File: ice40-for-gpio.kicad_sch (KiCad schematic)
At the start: 25 parts, among them U10 W25Q128JVS, U6 LP5907MFX-1.2, U9 ICE40UP5K-SG48ITR

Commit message: Update the schematic
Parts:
- added D6, D7: RED, LED_SMD:LED_0603_1608Metric, symbol Device:LED_Small
- added R34, R35: 1.2K, Resistor_SMD:R_0402_1005Metric, symbol Device:R_Small
- renumbered C32 to C20, C42 to C21, C33 to C22, C43 to C23, C35 to C24, C36 to C25, C34 to C26, C37 to C27, C19 to C28, C38 to C29, C39 to C30, C40 to C31, C20 to C32, C41 to C33, D9 to D5, R36 to R32, R45 to R33, R37 to R36, R38 to R37, R39 to R38, R40 to R39, U9 to U6, U10 to U7, U6 to U8
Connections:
- net GND: now also D6.1 (K), D7.1 (K)
- net ICE_LED1: now also R34.1
- net ICE_LED2: now also R35.1
- new net: D6.2 (A), R34.2
- new net: D7.2 (A), R35.2

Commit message: Update the source code
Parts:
- renumbered C20 to C18, C21 to C19, C22 to C20, C23 to C21, C24 to C22, C25 to C23, C26 to C24, C27 to C25, C28 to C26, C29 to C27, C30 to C28, C31 to C29, C32 to C30, C33 to C31, R32 to R38, R33 to R39, R34 to R40, R35 to R41, R36 to R42, R37 to R43, R38 to R44, R39 to R45, U6 to U5, U7 to U6, U8 to U7

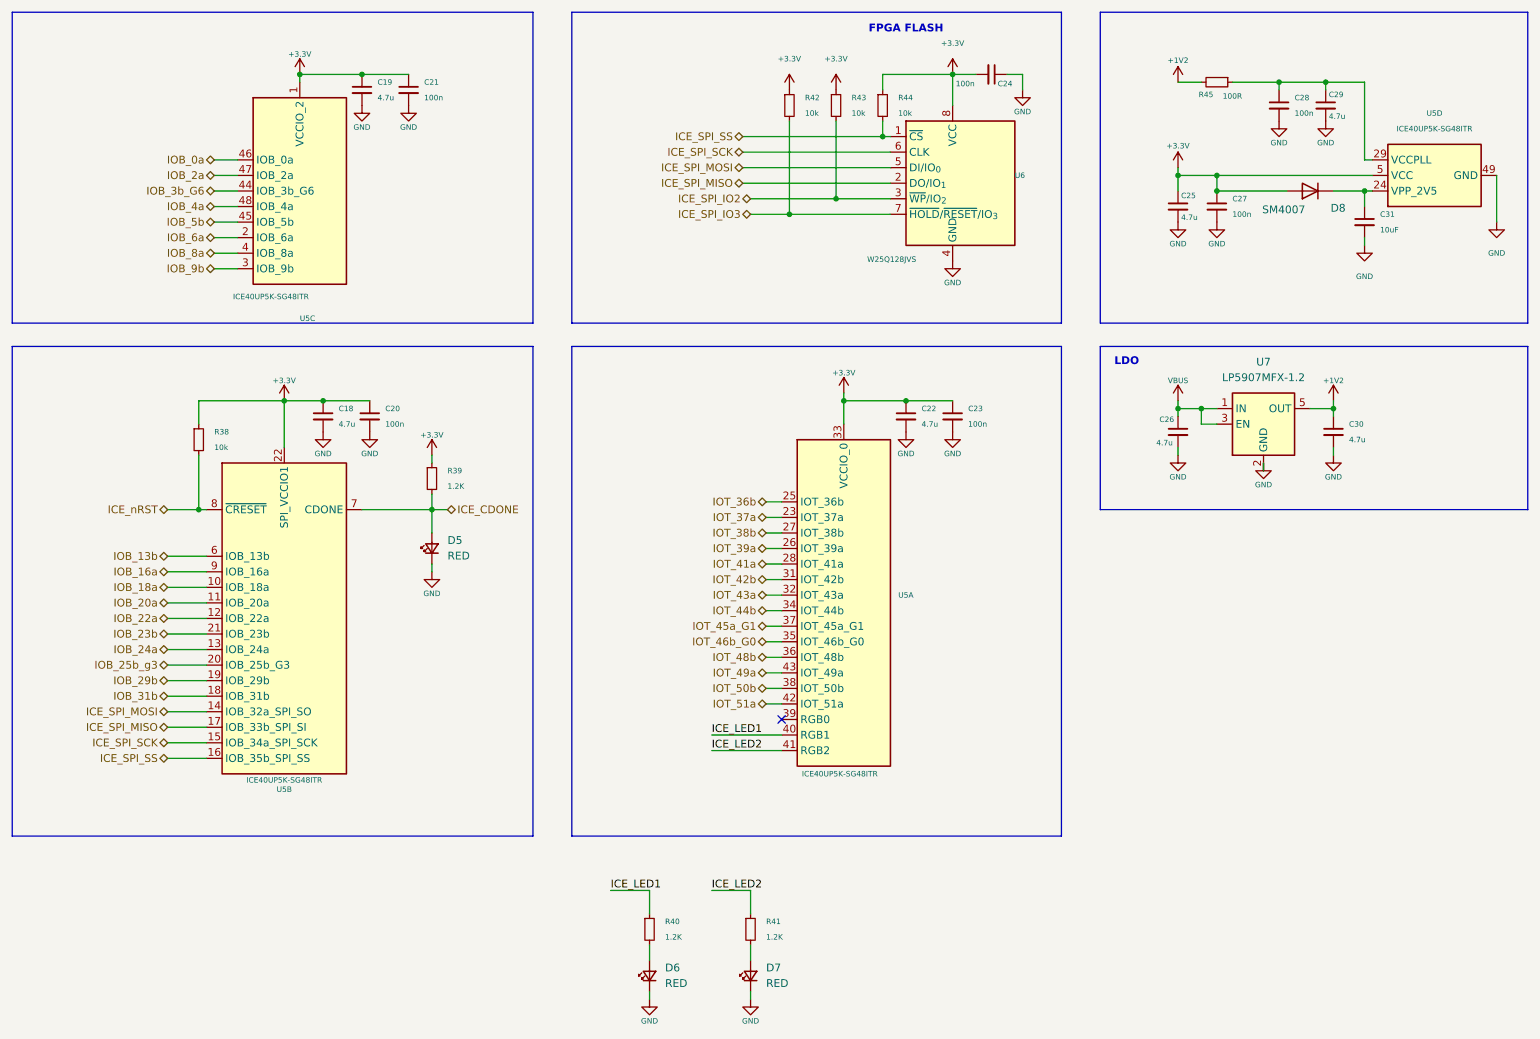
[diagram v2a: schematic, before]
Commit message: Update the footprints
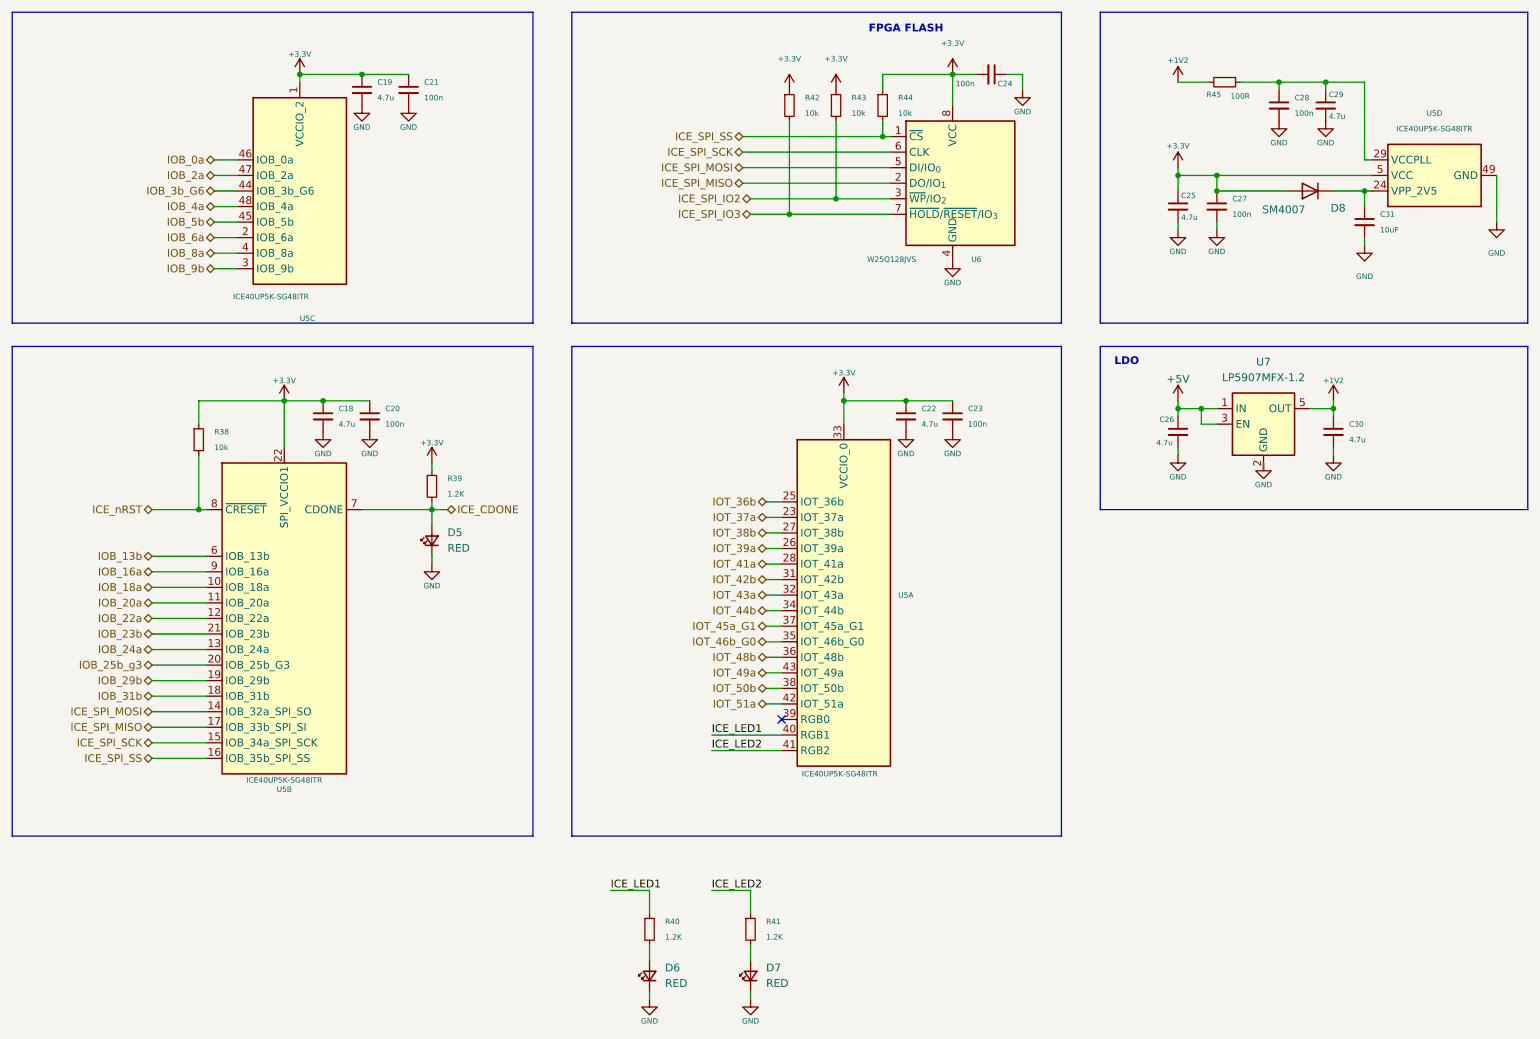
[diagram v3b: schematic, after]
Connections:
- net VBUS renamed +5V
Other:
- moved on the sheet: D5, R39, R45

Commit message: Update the BOM and the routing
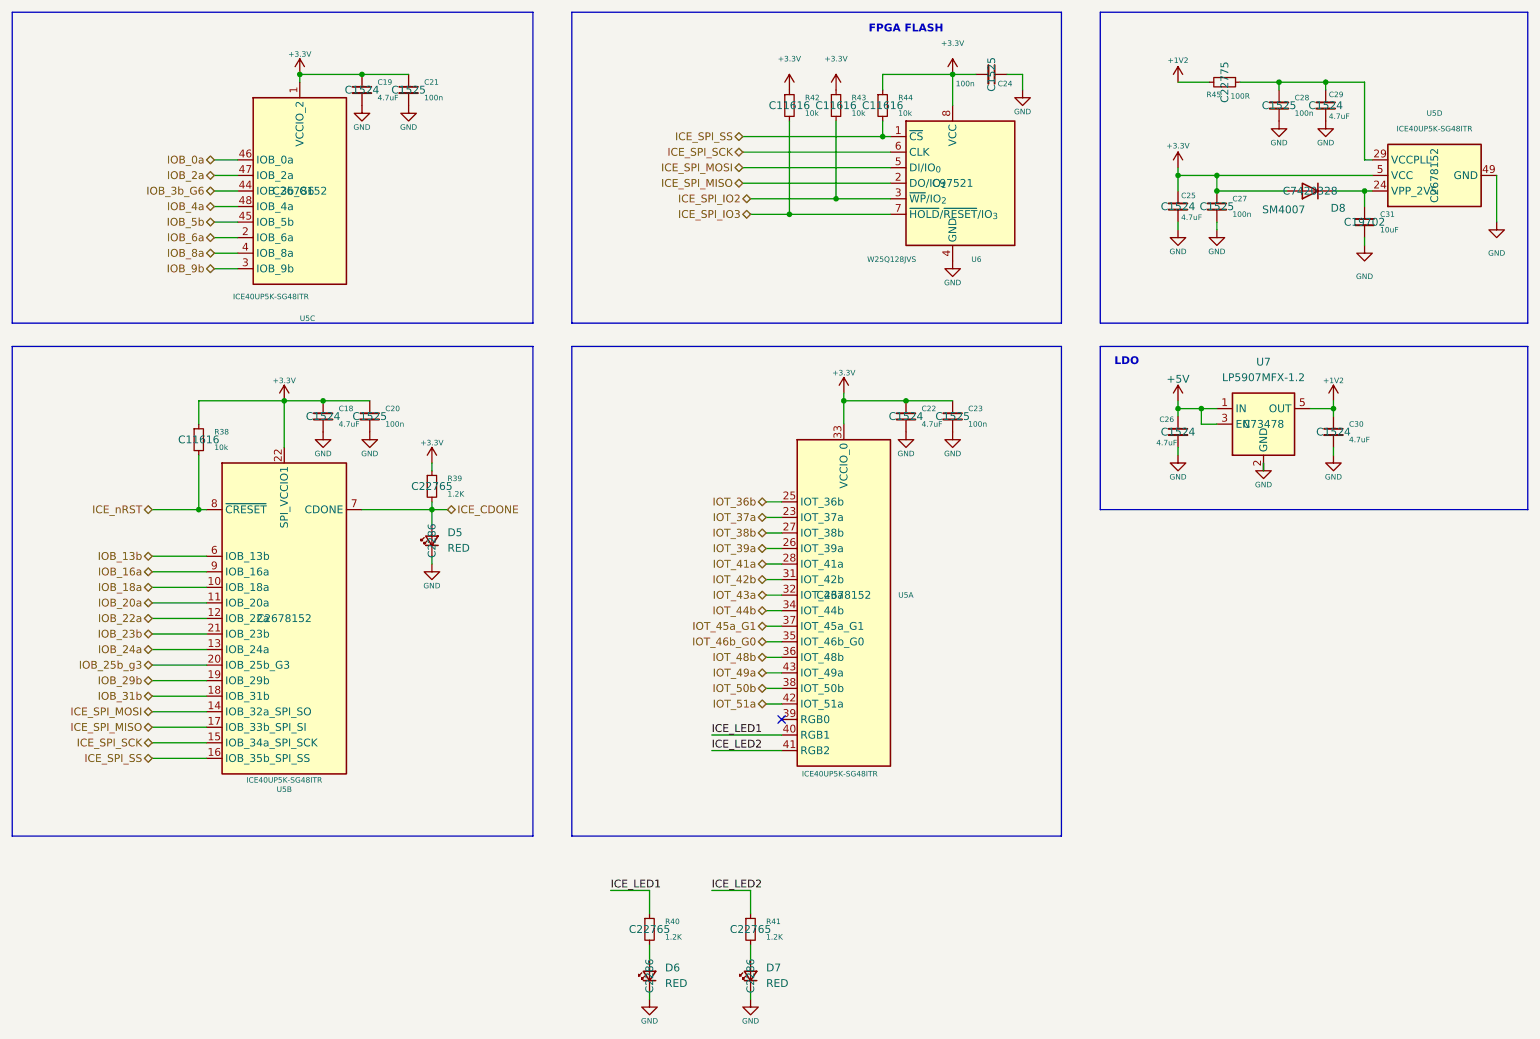
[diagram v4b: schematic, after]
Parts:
- C18, C19, C22, C25, C26, C29, C30: value 4.7u -> 4.7uF; LCSC (none) -> C1524
- C20, C21, C23, C24, C27, C28: LCSC (none) -> C1525
- C31: LCSC (none) -> C19702
- D5, D6, D7: LCSC (none) -> C2286
- D8: LCSC (none) -> C7420328
- R38, R42, R43, R44: LCSC (none) -> C11616
- R39, R40, R41: footprint Resistor_SMD:R_0402_1005Metric -> Resistor_SMD:R_0603_1608Metric; LCSC (none) -> C22765
- R45: footprint Resistor_SMD:R_0402_1005Metric -> Resistor_SMD:R_0603_1608Metric; LCSC (none) -> C22775
- U5: LCSC (none) -> C2678152
- U6: LCSC (none) -> C97521
- U7: LCSC (none) -> C73478

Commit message: Update the source files
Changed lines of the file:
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@@
 					(size 1.27 1.27)
 				)
+				(hide yes)
 			)
 		)
@@
 					(size 1.27 1.27)
 				)
+				(hide yes)
 			)
 		)
@@
 					(size 1.27 1.27)
 				)
+				(hide yes)
 			)
 		)
@@
 					(size 1.27 1.27)
 				)
+				(hide yes)
 			)
 		)
@@
 		(fields_autoplaced yes)
 		(property "Reference" "R39"
-			(at 93.98 96.5199 0)
+			(at 93.98 96.52 0)
 			(effects
 				(font
@@
 		)
 		(property "Value" "1.2K"
-			(at 93.98 99.0599 0)
+			(at 93.98 99.06 0)
 			(effects
 				(font
@@
 					(size 1.27 1.27)
 				)
+				(hide yes)
 			)
 		)
@@
 					(size 1.27 1.27)
 				)
+				(hide yes)
 			)
 		)
@@
 					(size 1.27 1.27)
 				)
+				(hide yes)
 			)
 		)
@@
 		(fields_autoplaced yes)
 		(property "Reference" "R38"
-			(at 55.88 88.8999 0)
+			(at 55.88 88.9 0)
 			(effects
 				(font
@@
 		)
 		(property "Value" "10k"
-			(at 55.88 91.4399 0)
+			(at 55.88 91.44 0)
 			(effects
 				(font
@@
 					(size 1.27 1.27)
 				)
+				(hide yes)
 			)
 		)
@@
 					(size 1.27 1.27)
 				)
+				(hide yes)
 			)
 		)

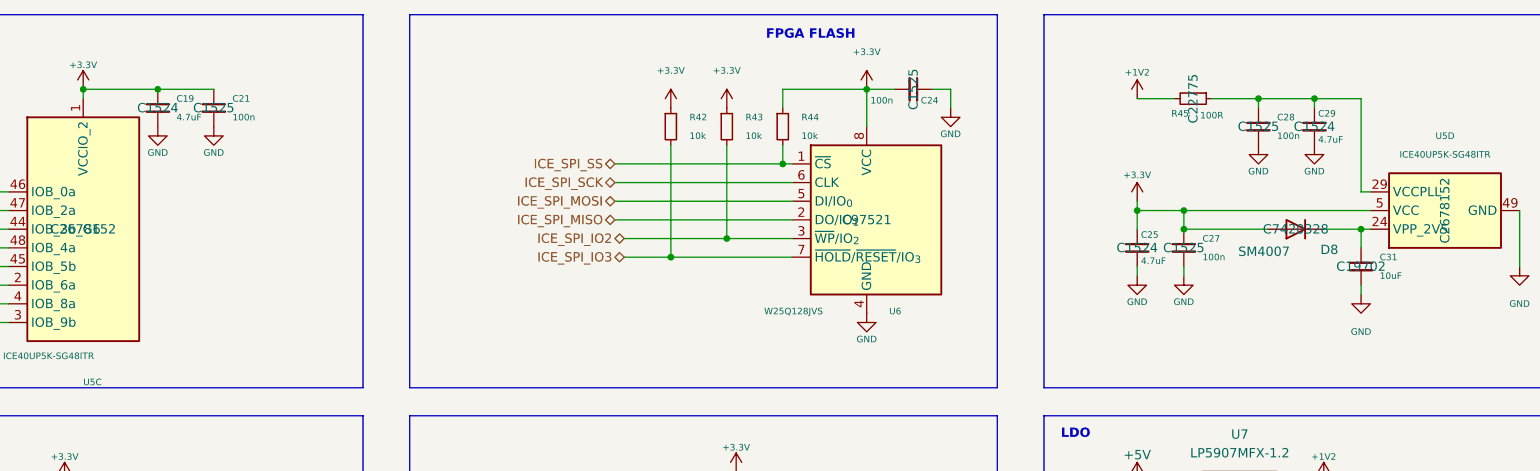
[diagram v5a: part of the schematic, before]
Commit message: Improve the routing
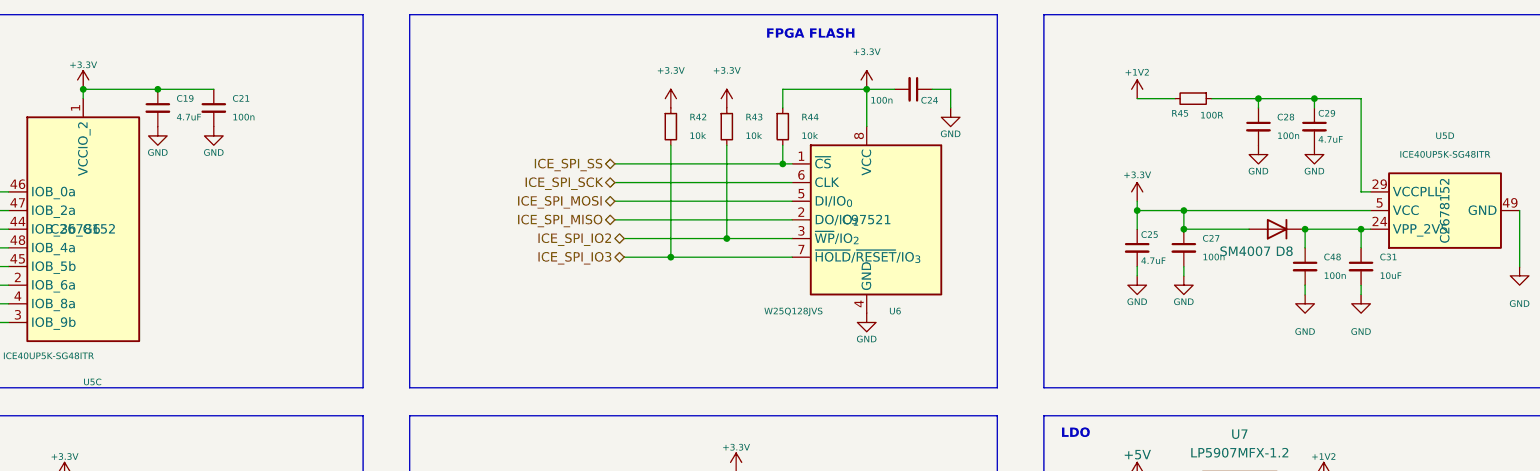
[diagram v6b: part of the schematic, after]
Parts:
- added C48: 100n, Capacitor_SMD:C_0402_1005Metric, symbol Device:C_Small
- R39: footprint Resistor_SMD:R_0603_1608Metric -> Resistor_SMD:R_0402_1005Metric
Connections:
- net GND: now also C48.2
- net at C31.1, D8.1 (K), U5.24 (VPP_2V5): now also C48.1
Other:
- moved on the sheet: D8
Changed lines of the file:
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@@
 	)
 	(junction
+		(at 236.22 49.53)
+		(diameter 0)
+		(color 0 0 0 0)
+	)
+	(junction
 		(at 158.75 83.82)
 		(diameter 0)
@@
 	(wire
 		(pts
+			(xy 236.22 49.53) (xy 236.22 52.07)
+		)
+		(stroke
+			(width 0)
+			(type default)
+		)
+	)
+	(wire
+		(pts
 			(xy 53.34 92.71) (xy 53.34 101.6)
 		)
@@
 	(wire
 		(pts
-			(xy 238.76 49.53) (xy 243.84 49.53)
+			(xy 236.22 49.53) (xy 243.84 49.53)
 		)
 		(stroke
@@
 	(wire
 		(pts
+			(xy 236.22 57.15) (xy 236.22 58.42)
+		)
+		(stroke
+			(width 0)
+			(type default)
+		)
+	)
+	(wire
+		(pts
 			(xy 237.49 31.75) (xy 237.49 33.02)
 		)
@@
 	(wire
 		(pts
-			(xy 231.14 49.53) (xy 219.71 49.53)
+			(xy 228.6 49.53) (xy 219.71 49.53)
 		)
 		(stroke
@@
 	(symbol
 		(lib_id "Diode:SM4007")
-		(at 234.95 49.53 180)
+		(at 232.41 49.53 180)
 		(unit 1)
 		(exclude_from_sim no)
@@
 		(dnp no)
 		(property "Reference" "D8"
-			(at 239.522 52.324 0)
+			(at 233.426 52.578 0)
 			(effects
 				(font
@@
 		)
 		(property "Value" "SM4007"
-			(at 230.632 52.578 0)
+			(at 228.092 52.578 0)
 			(effects
 				(font
@@
 		)
 		(property "Footprint" "Diode_SMD:D_SOD-123F"
-			(at 234.95 45.085 0)
+			(at 232.41 45.085 0)
 			(effects
 				(font
@@
 		)
 		(property "Datasheet" "http://cdn-reichelt.de/documents/datenblatt/A400/SMD1N400%23DIO.pdf"
-			(at 234.95 49.53 0)
+			(at 232.41 49.53 0)
 			(effects
 				(font
@@
 		)
 		(property "Description" "1000V 1A General Purpose Rectifier Diode, MELF"
-			(at 234.95 49.53 0)
+			(at 232.41 49.53 0)
 			(effects
 				(font
@@
 		)
 		(property "LCSC" "C7420328"
-			(at 234.95 49.53 0)
+			(at 232.41 49.53 0)
 			(effects
 				(font
 					(size 1.27 1.27)
 				)
+				(hide yes)
 			)
 		)
@@
 		(fields_autoplaced yes)
 		(property "Reference" "C21"
-			(at 90.17 31.7562 0)
+			(at 90.17 31.7563 0)
 			(effects
 				(font
@@
 		)
 		(property "Value" "100n"
-			(at 90.17 34.2962 0)
+			(at 90.17 34.2963 0)
 			(effects
 				(font
@@
 					(size 1.27 1.27)
 				)
+				(hide yes)
 			)
 		)
@@
 		(fields_autoplaced yes)
 		(property "Reference" "C27"
-			(at 222.25 50.8062 0)
+			(at 222.25 50.8063 0)
 			(effects
 				(font
@@
 		)
 		(property "Value" "100n"
-			(at 222.25 53.3462 0)
+			(at 222.25 53.3463 0)
 			(effects
 				(font
@@
 					(size 1.27 1.27)
 				)
+				(hide yes)
 			)
 		)
@@
 					(size 1.27 1.27)
 				)
+				(hide yes)
 			)
 		)
@@
 					(size 1.27 1.27)
 				)
+				(hide yes)
 			)
 		)
@@
 					(size 1.27 1.27)
 				)
+				(hide yes)
 			)
 		)
@@
 		(fields_autoplaced yes)
 		(property "Reference" "C31"
-			(at 246.38 53.3462 0)
+			(at 246.38 53.3463 0)
 			(effects
 				(font
@@
 		)
 		(property "Value" "10uF"
-			(at 246.38 55.8862 0)
+			(at 246.38 55.8863 0)
 			(effects
 				(font
@@
 					(size 1.27 1.27)
 				)
+				(hide yes)
 			)
 		)
@@
 	)
 	(symbol
+		(lib_id "power:GND")
+		(at 236.22 58.42 0)
+		(mirror y)
+		(unit 1)
+		(exclude_from_sim no)
+		(in_bom yes)
+		(on_board yes)
+		(dnp no)
+		(fields_autoplaced yes)
+		(property "Reference" "#PWR0157"
+			(at 236.22 64.77 0)
+			(effects
+				(font
+					(size 0.889 0.889)
+				)
+				(hide yes)
+			)
+		)
+		(property "Value" "GND"
+			(at 236.22 63.5 0)
+			(effects
+				(font
+					(size 0.889 0.889)
+				)
+			)
+		)
+		(property "Footprint" ""
+			(at 236.22 58.42 0)
+			(effects
+				(font
+					(size 1.27 1.27)
+				)
+				(hide yes)
+			)
+		)
+		(property "Datasheet" ""
+			(at 236.22 58.42 0)
+			(effects
+				(font
+					(size 1.27 1.27)
+				)
+				(hide yes)
+			)
+		)
+		(property "Description" "Power symbol creates a global label with name \"GND\" , ground"
+			(at 236.22 58.42 0)
+			(effects
+				(font
+					(size 1.27 1.27)
+				)
+				(hide yes)
+			)
+		)
+		(pin "1"
+		)
+		(instances
+			(project "stm32-fpga-bootloader"
+				(path "/5ed49623-6cbc-4a61-8fb3-1814d185ddb6/f3632bef-2b61-47cc-a59f-7ffc5c491629"
+					(reference "#PWR0157")
+					(unit 1)
+				)
+			)
+		)
+	)
+	(symbol
 		(lib_id "power:+3.3V")
 		(at 158.75 82.55 0)
@@
 	)
 	(symbol
+		(lib_id "Device:C_Small")
+		(at 236.22 54.61 0)
+		(unit 1)
+		(exclude_from_sim no)
+		(in_bom yes)
+		(on_board yes)
+		(dnp no)
+		(fields_autoplaced yes)
+		(property "Reference" "C48"
+			(at 238.76 53.3463 0)
+			(effects
+				(font
+					(size 0.889 0.889)
+				)
+				(justify left)
+			)
+		)
+		(property "Value" "100n"
+			(at 238.76 55.8863 0)
+			(effects
+				(font
+					(size 0.889 0.889)
+				)
+				(justify left)
+			)
+		)
+		(property "Footprint" "Capacitor_SMD:C_0402_1005Metric"
+			(at 236.22 54.61 0)
+			(effects
+				(font
+					(size 1.27 1.27)
+				)
+				(hide yes)
+			)
+		)
+		(property "Datasheet" "~"
+			(at 236.22 54.61 0)
+			(effects
+				(font
+					(size 1.27 1.27)
+				)
+				(hide yes)
+			)
+		)
+		(property "Description" "Unpolarized capacitor, small symbol"
+			(at 236.22 54.61 0)
+			(effects
+				(font
+					(size 1.27 1.27)
+				)
+				(hide yes)
+			)
+		)
+		(property "LCSC" "C1525 "
+			(at 236.22 54.61 0)
+			(effects
+				(font
+					(size 1.27 1.27)
+				)
+				(hide yes)
+			)
+		)
+		(pin "2"
+		)
+		(pin "1"
+		)
+		(instances
+			(project "stm32-fpga-bootloader"
+				(path "/5ed49623-6cbc-4a61-8fb3-1814d185ddb6/f3632bef-2b61-47cc-a59f-7ffc5c491629"
+					(reference "C48")
+					(unit 1)
+				)
+			)
+		)
+	)
+	(symbol
 		(lib_id "Device:R_Small")
 		(at 91.44 97.79 0)
@@
 			)
 		)
-		(property "Footprint" "Resistor_SMD:R_0603_1608Metric"
+		(property "Footprint" "Resistor_SMD:R_0402_1005Metric"
 			(at 91.44 97.79 0)
 			(effects
@@
 		(fields_autoplaced yes)
 		(property "Reference" "C28"
-			(at 232.41 34.2962 0)
+			(at 232.41 34.2963 0)
 			(effects
 				(font
@@
 		)
 		(property "Value" "100n"
-			(at 232.41 36.8362 0)
+			(at 232.41 36.8363 0)
 			(effects
 				(font
@@
 					(size 1.27 1.27)
 				)
+				(hide yes)
 			)
 		)
@@
 					(size 1.27 1.27)
 				)
+				(hide yes)
 			)
 		)
@@
 					(size 1.27 1.27)
 				)
+				(hide yes)
 			)
 		)
